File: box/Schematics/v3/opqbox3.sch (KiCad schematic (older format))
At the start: 11 parts

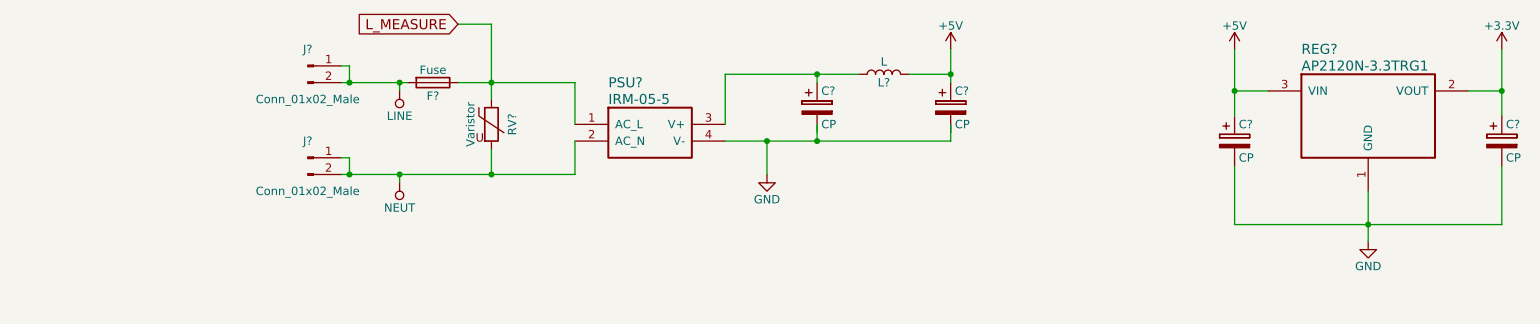
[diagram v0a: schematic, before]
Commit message: fix ERC errors
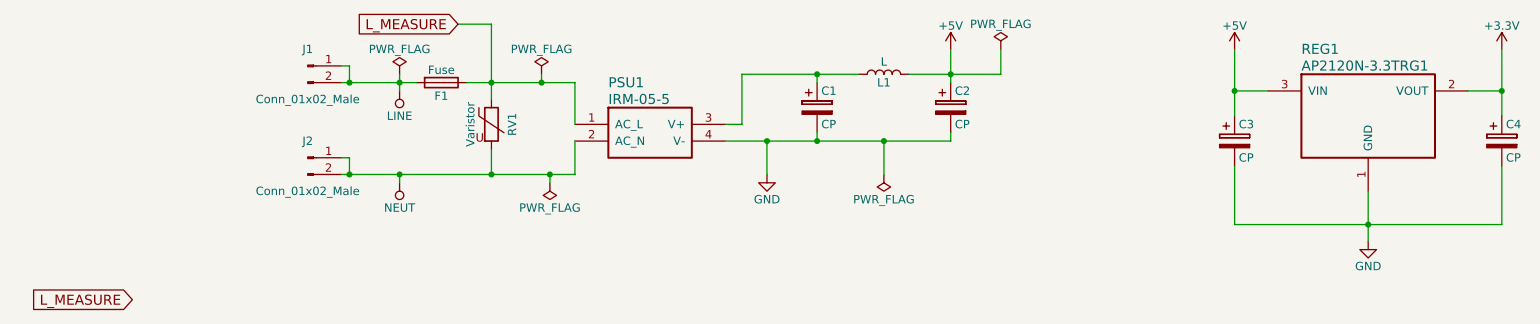
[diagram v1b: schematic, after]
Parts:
- gave numbers to parts that had none: 11
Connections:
- wire segments 31 -> 36
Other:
- moved on the sheet: F1
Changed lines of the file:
@@
 $EndDescr
 $Comp
-L GND #PWR?
+L GND #PWR01
 U 1 1 5A823328
 P 8850 3150
-F 0 "#PWR?" H 8850 2900 50  0001 C CNN
+F 0 "#PWR01" H 8850 2900 50  0001 C CNN
 F 1 "GND" H 8850 3000 50  0000 C CNN
 F 2 "" H 8850 3150 50  0001 C CNN
@@
 	1    0    0    -1
 $EndComp
-Wire Wire Line
-	8850 2850 8850 3150
-$Comp
-L CP C?
+$Comp
+L CP C3
 U 1 1 5A823341
 P 8050 2550
-F 0 "C?" H 8075 2650 50  0000 L CNN
+F 0 "C3" H 8075 2650 50  0000 L CNN
 F 1 "CP" H 8075 2450 50  0000 L CNN
 F 2 "" H 8088 2400 50  0001 C CNN
@@
 $EndComp
 $Comp
-L CP C?
+L CP C4
 U 1 1 5A82336C
 P 9650 2550
-F 0 "C?" H 9675 2650 50  0000 L CNN
+F 0 "C4" H 9675 2650 50  0000 L CNN
 F 1 "CP" H 9675 2450 50  0000 L CNN
 F 2 "" H 9688 2400 50  0001 C CNN
@@
 $EndComp
 Wire Wire Line
-	8050 2000 8050 2400
-Wire Wire Line
-	8050 2250 8250 2250
-Wire Wire Line
 	9650 2000 9650 2400
 Wire Wire Line
@@
 	9650 3050 9650 2700
 $Comp
-L AP2120N-3.3TRG1 REG?
+L AP2120N-3.3TRG1 REG1
 U 1 1 5A823602
 P 8250 2250
-F 0 "REG?" H 8450 2500 60  0000 L CNN
+F 0 "REG1" H 8450 2500 60  0000 L CNN
 F 1 "AP2120N-3.3TRG1" H 8450 2400 60  0000 L CNN
 F 2 "" H 8250 2250 60  0001 C CNN
@@
 $EndComp
 $Comp
-L +5V #PWR?
+L +5V #PWR02
 U 1 1 5A8236B0
 P 8050 2000
-F 0 "#PWR?" H 8050 1850 50  0001 C CNN
+F 0 "#PWR02" H 8050 1850 50  0001 C CNN
 F 1 "+5V" H 8050 2140 50  0000 C CNN
 F 2 "" H 8050 2000 50  0001 C CNN
@@
 $EndComp
 $Comp
-L +3.3V #PWR?
+L +3.3V #PWR03
 U 1 1 5A8236CA
 P 9650 2000
-F 0 "#PWR?" H 9650 1850 50  0001 C CNN
+F 0 "#PWR03" H 9650 1850 50  0001 C CNN
 F 1 "+3.3V" H 9650 2140 50  0000 C CNN
 F 2 "" H 9650 2000 50  0001 C CNN
@@
 Connection ~ 9650 2250
 $Comp
-L Fuse F?
+L Fuse F1
 U 1 1 5A823CA9
-P 3250 2200
-F 0 "F?" V 3330 2200 50  0000 C CNN
-F 1 "Fuse" V 3175 2200 50  0000 C CNN
-F 2 "" V 3180 2200 50  0001 C CNN
-F 3 "" H 3250 2200 50  0001 C CNN
-	1    3250 2200
+P 3300 2200
+F 0 "F1" V 3380 2200 50  0000 C CNN
+F 1 "Fuse" V 3225 2200 50  0000 C CNN
+F 2 "" V 3230 2200 50  0001 C CNN
+F 3 "" H 3300 2200 50  0001 C CNN
+	1    3300 2200
 	0    1    1    0
 $EndComp
-Wire Wire Line
-	2700 2200 3100 2200
-$Comp
-L Varistor RV?
+$Comp
+L Varistor RV1
 U 1 1 5A823D68
 P 3600 2450
-F 0 "RV?" V 3725 2450 50  0000 C CNN
+F 0 "RV1" V 3725 2450 50  0000 C CNN
 F 1 "Varistor" V 3475 2450 50  0000 C CNN
 F 2 "" V 3530 2450 50  0001 C CNN
@@
 $EndComp
 Wire Wire Line
-	3400 2200 4100 2200
-Wire Wire Line
 	3600 1850 3600 2300
 Wire Wire Line
@@
 Connection ~ 3600 2750
 $Comp
-L IRM-05-5 PSU?
+L IRM-05-5 PSU1
 U 1 1 5A82394D
 P 4100 2450
-F 0 "PSU?" H 4300 2700 60  0000 L CNN
+F 0 "PSU1" H 4300 2700 60  0000 L CNN
 F 1 "IRM-05-5" H 4300 2600 60  0000 L CNN
 F 2 "" H 4100 2450 60  0001 C CNN
@@
 $EndComp
 $Comp
-L GND #PWR?
+L GND #PWR04
 U 1 1 5A823A0C
 P 5250 2750
-F 0 "#PWR?" H 5250 2500 50  0001 C CNN
+F 0 "#PWR04" H 5250 2500 50  0001 C CNN
 F 1 "GND" H 5250 2600 50  0000 C CNN
 F 2 "" H 5250 2750 50  0001 C CNN
@@
 Wire Wire Line
 	5250 2550 5250 2750
-Wire Wire Line
-	5000 2150 5000 2450
-$Comp
-L CP C?
+$Comp
+L CP C1
 U 1 1 5A823A87
 P 5550 2350
-F 0 "C?" H 5575 2450 50  0000 L CNN
+F 0 "C1" H 5575 2450 50  0000 L CNN
 F 1 "CP" H 5575 2250 50  0000 L CNN
 F 2 "" H 5588 2200 50  0001 C CNN
@@
 $EndComp
 $Comp
-L CP C?
+L CP C2
 U 1 1 5A823ADE
 P 6350 2350
-F 0 "C?" H 6375 2450 50  0000 L CNN
+F 0 "C2" H 6375 2450 50  0000 L CNN
 F 1 "CP" H 6375 2250 50  0000 L CNN
 F 2 "" H 6388 2200 50  0001 C CNN
@@
 $EndComp
 $Comp
-L L L?
+L L L1
 U 1 1 5A823B3B
 P 5950 2150
-F 0 "L?" V 5900 2150 50  0000 C CNN
+F 0 "L1" V 5900 2150 50  0000 C CNN
 F 1 "L" V 6025 2150 50  0000 C CNN
 F 2 "" H 5950 2150 50  0001 C CNN
@@
 $EndComp
 Wire Wire Line
-	6100 2150 6350 2150
-Wire Wire Line
-	5000 2150 5800 2150
-Wire Wire Line
-	5550 2550 5550 2450
+	6100 2150 6650 2150
 Connection ~ 5250 2550
-Wire Wire Line
-	6350 2550 6350 2450
 Connection ~ 5550 2550
 Connection ~ 5550 2150
 Wire Wire Line
-	6350 2000 6350 2200
-Wire Wire Line
 	5550 2200 5550 2150
 $Comp
-L +5V #PWR?
+L +5V #PWR05
 U 1 1 5A823E92
 P 6350 2000
-F 0 "#PWR?" H 6350 1850 50  0001 C CNN
+F 0 "#PWR05" H 6350 1850 50  0001 C CNN
 F 1 "+5V" H 6350 2140 50  0000 C CNN
 F 2 "" H 6350 2000 50  0001 C CNN
@@
 	3400 1850 3600 1850
 $Comp
-L NEUT #PWR?
+L NEUT #PWR06
 U 1 1 5A824199
 P 3050 2800
-F 0 "#PWR?" H 3050 2650 50  0001 C CNN
+F 0 "#PWR06" H 3050 2650 50  0001 C CNN
 F 1 "NEUT" H 3050 2950 50  0000 C CNN
 F 2 "" H 3050 2800 50  0001 C CNN
@@
 Connection ~ 3050 2750
 $Comp
-L LINE #PWR?
+L LINE #PWR07
 U 1 1 5A82420A
 P 3050 2250
-F 0 "#PWR?" H 3050 2100 50  0001 C CNN
+F 0 "#PWR07" H 3050 2100 50  0001 C CNN
 F 1 "LINE" H 3050 2400 50  0000 C CNN
 F 2 "" H 3050 2250 50  0001 C CNN
@@
 $EndComp
 Connection ~ 3050 2200
-Wire Wire Line
-	3050 2800 3050 2750
-Wire Wire Line
-	3050 2250 3050 2200
-$Comp
-L Conn_01x02_Male J?
+$Comp
+L Conn_01x02_Male J1
 U 1 1 5A8248C2
 P 2500 2100
-F 0 "J?" H 2500 2200 50  0000 C CNN
+F 0 "J1" H 2500 2200 50  0000 C CNN
 F 1 "Conn_01x02_Male" H 2500 1900 50  0000 C CNN
 F 2 "" H 2500 2100 50  0001 C CNN
@@
 $EndComp
 $Comp
-L Conn_01x02_Male J?
+L Conn_01x02_Male J2
 U 1 1 5A82497D
 P 2500 2650
-F 0 "J?" H 2500 2750 50  0000 C CNN
+F 0 "J2" H 2500 2750 50  0000 C CNN
 F 1 "Conn_01x02_Male" H 2500 2450 50  0000 C CNN
 F 2 "" H 2500 2650 50  0001 C CNN
@@
 	2750 2650 2750 2750
 Connection ~ 2750 2750
+Wire Wire Line
+	5550 2550 5550 2500
+Wire Wire Line
+	6350 2550 6350 2500
+Wire Wire Line
+	8250 2250 8050 2250
+Wire Wire Line
+	8850 2850 8850 3150
+Wire Wire Line
+	6350 2000 6350 2200
+Wire Wire Line
+	8050 2000 8050 2400
+$Comp
+L PWR_FLAG #FLG08
+U 1 1 5A825B85
+P 3950 2800
+F 0 "#FLG08" H 3950 2875 50  0001 C CNN
+F 1 "PWR_FLAG" H 3950 2950 50  0000 C CNN
+F 2 "" H 3950 2800 50  0001 C CNN
+F 3 "" H 3950 2800 50  0001 C CNN
+	1    3950 2800
+	-1   0    0    1
+$EndComp
+$Comp
+L PWR_FLAG #FLG09
+U 1 1 5A825D4F
+P 3900 2150
+F 0 "#FLG09" H 3900 2225 50  0001 C CNN
+F 1 "PWR_FLAG" H 3900 2300 50  0000 C CNN
+F 2 "" H 3900 2150 50  0001 C CNN
+F 3 "" H 3900 2150 50  0001 C CNN
+	1    3900 2150
+	1    0    0    -1
+$EndComp
+Wire Wire Line
+	2700 2200 3150 2200
+Wire Wire Line
+	3450 2200 4100 2200
+Wire Wire Line
+	3050 2150 3050 2250
+Wire Wire Line
+	3050 2800 3050 2750
+Wire Wire Line
+	3950 2800 3950 2750
+Connection ~ 3950 2750
+Wire Wire Line
+	3900 2150 3900 2200
+Connection ~ 3900 2200
+$Comp
+L PWR_FLAG #FLG010
+U 1 1 5A826550
+P 6650 2000
+F 0 "#FLG010" H 6650 2075 50  0001 C CNN
+F 1 "PWR_FLAG" H 6650 2150 50  0000 C CNN
+F 2 "" H 6650 2000 50  0001 C CNN
+F 3 "" H 6650 2000 50  0001 C CNN
+	1    6650 2000
+	1    0    0    -1
+$EndComp
+Wire Wire Line
+	6650 2150 6650 2000
+$Comp
+L PWR_FLAG #FLG011
+U 1 1 5A82679F
+P 3050 2150
+F 0 "#FLG011" H 3050 2225 50  0001 C CNN
+F 1 "PWR_FLAG" H 3050 2300 50  0000 C CNN
+F 2 "" H 3050 2150 50  0001 C CNN
+F 3 "" H 3050 2150 50  0001 C CNN
+	1    3050 2150
+	1    0    0    -1
+$EndComp
+$Comp
+L PWR_FLAG #FLG012
+U 1 1 5A8268AF
+P 5950 2750
+F 0 "#FLG012" H 5950 2825 50  0001 C CNN
+F 1 "PWR_FLAG" H 5950 2900 50  0000 C CNN
+F 2 "" H 5950 2750 50  0001 C CNN
+F 3 "" H 5950 2750 50  0001 C CNN
+	1    5950 2750
+	-1   0    0    1
+$EndComp
+Wire Wire Line
+	5950 2750 5950 2550
+Connection ~ 5950 2550
+Wire Wire Line
+	5000 2450 5100 2450
+Wire Wire Line
+	5100 2450 5100 2150
+Wire Wire Line
+	5100 2150 5800 2150
+Text GLabel 1450 3500 0    60   Input ~ 0
+L_MEASURE
 $EndSCHEMATC

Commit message: finish power schematic
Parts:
- added C10, C11, C5, C6, C7, C8, C9: C, symbol C
- added F2: Fuse, symbol Fuse
- added R1, R2, R3, R4, R5, R6, R7, R8, R9: R, symbol R
- added U1: AMC1100DWV, symbol AMC1100DWV
- added U2: ADUM5010ARSZ, symbol ADUM5010ARSZ
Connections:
- net +3V3: now also C10.1, U1.8 (VDD2)
- net +5V: now also C8.1, C9.1, U2.9 (VIN)
- net GND: now also C10.2, C8.2, C9.2, R7.2, U1.5 (GND2), U2.10 (GND1), U2.2 (GND1), U2.5 (GND1), U2.6 (GND1)
- net L_MEASURE: now also F2.2
- net NEUT: now also C5.2, C7.2, R2.2, R4.2, R6.2, U1.4 (GND1), U2.11 (GND2), U2.15 (GND2), U2.16 (GND2), U2.19 (GND2)
- new net: C6.1, R3.1, U1.2 (VINP)
- new net: C6.2, R4.1, U1.3 (VINN)
- new net: R9.2, U1.6 (VOUTN)
- new net: R8.2, U1.7 (VOUTP)
- new net: F2.1, R1.1
- new net: R1.2, R2.1, R3.2
- new net: R5.2, R6.1, U2.13 (VSEL)
- new net: R7.1, U2.8 (nENABLE)
- new net 5V_UNISOLATED: C5.1, C7.1, R5.1, U1.1 (VDD1), U2.12 (VOUT)
- new net ADC_IN+: C11.1, R8.1
- new net ADC_IN-: C11.2, R9.1
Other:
- note added: "Isolated"
- note added: "NOT isolated"
- moved on the sheet: C1, C2, C3, C4, F1, J1, J2, L1, PSU1, REG1, RV1

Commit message: setup heirarchical sheets
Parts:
- removed C1, C2, C3, C4: CP, symbol CP
- removed C10, C11, C5, C6, C7, C8, C9: C, symbol C
- removed F1, F2: Fuse, symbol Fuse
- removed L1: L, symbol L
- removed PSU1: IRM-05-5, symbol IRM-05-5
- removed R1, R2, R3, R4, R5, R6, R7, R8, R9: R, symbol R
- removed REG1: AP2120N-3.3TRG1, symbol AP2120N-3.3TRG1
- removed RV1: Varistor, symbol Varistor
- removed U1: AMC1100DWV, symbol AMC1100DWV
- removed U2: ADUM5010ARSZ, symbol ADUM5010ARSZ
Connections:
- net LINE renamed power/LINE
- net NEUT renamed power/NEUTRAL

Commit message: finish dsp schematics
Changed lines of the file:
@@
 LIBS:conn
 LIBS:contrib
+LIBS:stm32
 LIBS:opqbox3-cache
 EELAYER 25 0
@@
 $Descr A4 11693 8268
 encoding utf-8
-Sheet 1 2
+Sheet 1 3
 Title ""
 Date ""
@@
 $EndDescr
 $Sheet
-S 2150 1200 1500 1050
+S 2150 1200 1550 1600
 U 5A829EE9
 F0 "power" 60
@@
 F2 "LINE" I L 2150 1500 60
 F3 "NEUTRAL" I L 2150 1950 60
-F4 "ADC_IN+" O R 3650 1350 60
-F5 "ADC_IN-" O R 3650 1500 60
-F6 "+3.3V" O R 3650 2000 60
-F7 "+5V" O R 3650 1850 60
-F8 "GND" O R 3650 2150 60
+F4 "+3.3V" O R 3700 2500 60
+F5 "+5V" O R 3700 2350 60
+F6 "GND" O R 3700 2650 60
+F7 "3.3VREF" O R 3700 1950 60
+F8 "ADC" O R 3700 1350 60
 $EndSheet
 Wire Notes Line
@@
 	1900 1450 1900 1500
 Connection ~ 1900 1500
-Text Notes 3000 2600 0    60   ~ 0
+Text Notes 3050 3150 0    60   ~ 0
 Isolated
-Text Notes 2200 2600 0    60   ~ 0
+Text Notes 2150 3150 0    60   ~ 0
 NOT isolated
+$Sheet
+S 4300 1200 1600 1600
+U 5A835DDE
+F0 "dsp" 60
+F1 "dsp.sch" 60
+F2 "3.3VREF" I L 4300 1950 60
+F3 "SPI" B R 5900 1650 60
+F4 "JTAG" B R 5900 1800 60
+F5 "UART" B R 5900 2000 60
+F6 "PPS" O R 5900 2600 60
+F7 "LED" O R 5900 2450 60
+F8 "BOOT_MODE" I L 4300 2600 60
+F9 "VBAT" I L 4300 2400 60
+F10 "FLAG1" B R 5900 2250 60
+F11 "ADC" I L 4300 1350 60
+$EndSheet
+Wire Wire Line
+	3700 1950 4300 1950
+Wire Bus Line
+	3700 1350 4300 1350
 $EndSCHEMATC
